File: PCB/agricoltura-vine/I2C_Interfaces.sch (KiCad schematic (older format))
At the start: 11 parts, among them T10 BM04B-SRSS-TB(LF)(SN), T11 BM04B-SRSS-TB(LF)(SN), T12 BM04B-SRSS-TB(LF)(SN), T13 BM04B-SRSS-TB(LF)(SN), T14 BM04B-SRSS-TB(LF)(SN), T15 BM04B-SRSS-TB(LF)(SN), T8 BM04B-SRSS-TB(LF)(SN), T9 BM04B-SRSS-TB(LF)(SN), U3 TCA9548APWR

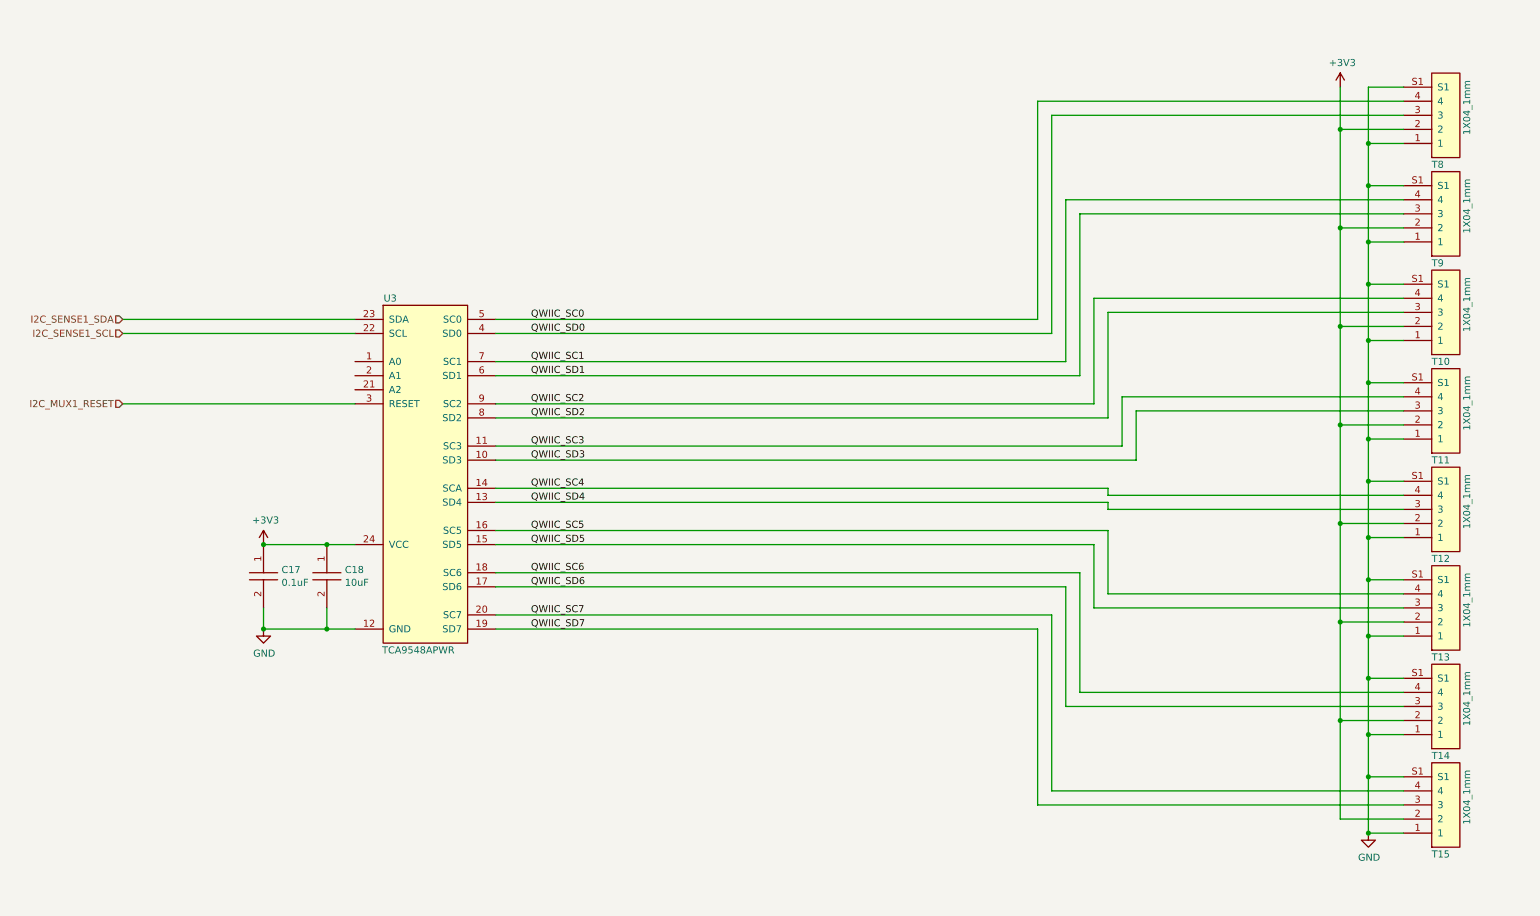
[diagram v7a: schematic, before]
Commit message: Added EEProm
Eeprom added and routed in circuit board, USB resitors added. TVS diodes and pullups added to I2C ports not yet placed.
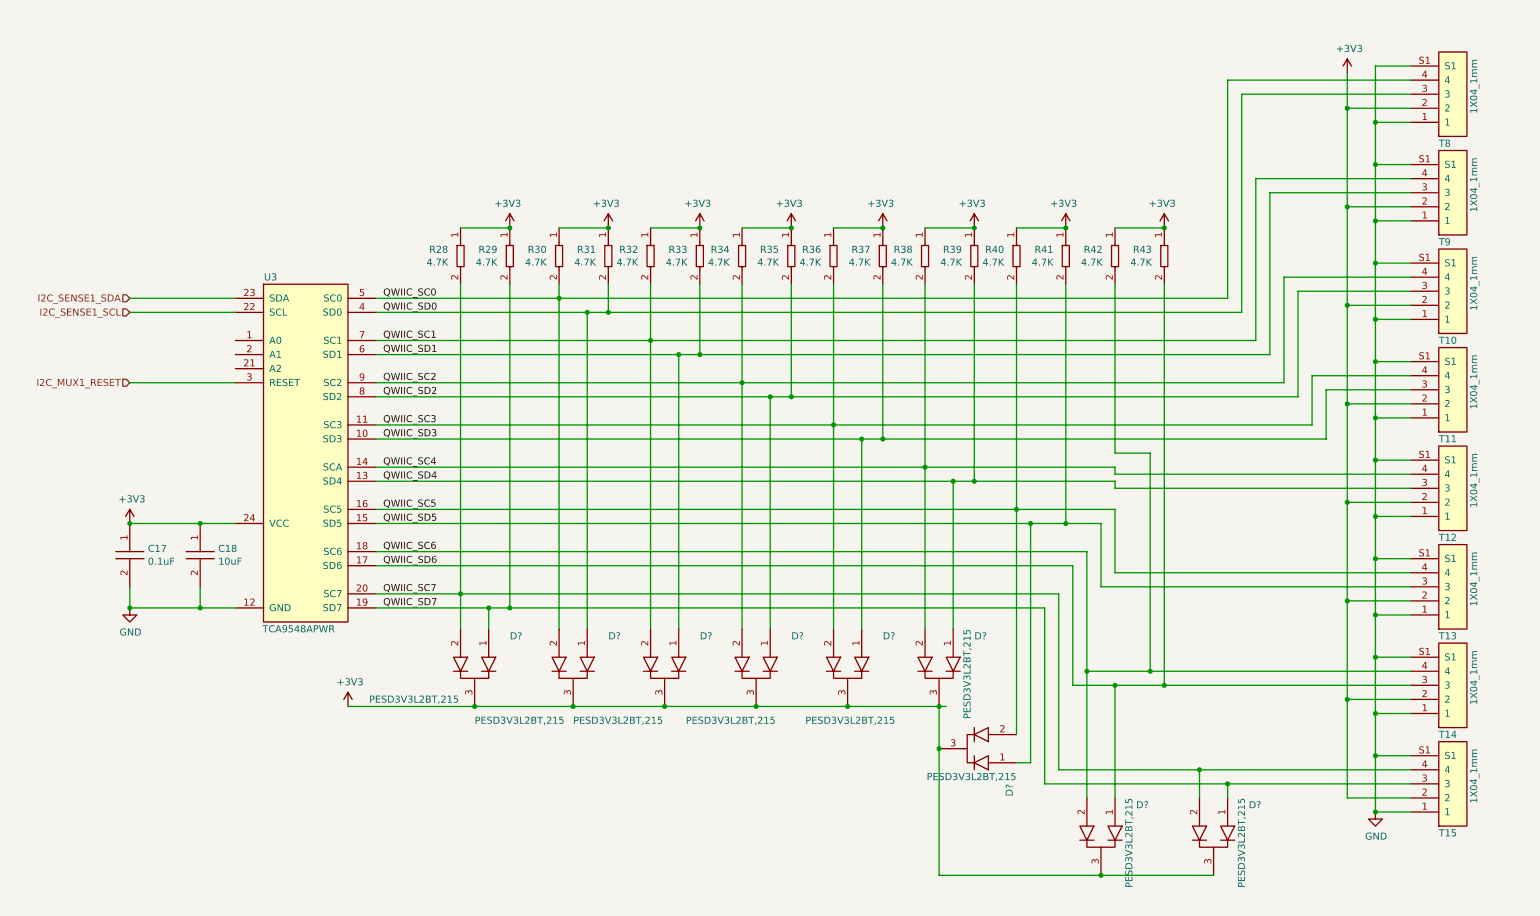
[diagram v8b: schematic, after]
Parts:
- added D? (x9): PESD3V3L2BT,215, AVR-KiCAD-Lib-Diodes:SOT-23, symbol AVR-KiCAD-Lib-Diodes:PESD3V3L2BT,215
- added R28, R29, R30, R31, R32, R33, R34, R35, R36, R37, R38, R39, R40, R41, R42, R43: RC0402FR-074K7L, AVR-KiCAD-Lib-Resistors:R0402, symbol AVR-KiCAD-Lib-Resistors:RC0402FR-074K7L
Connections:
- net +3V3: now also D?.3, D?.3, D?.3, D?.3, D?.3, D?.3, D?.3, D?.3, D?.3, R28.1, R29.1, R30.1, R31.1, R32.1, R33.1, R34.1, R35.1, R36.1, R37.1, R38.1, R39.1, R40.1, R41.1, R42.1, R43.1
- net QWIIC_SC0: now also D?.2, R30.2
- net QWIIC_SC1: now also D?.2, R32.2
- net QWIIC_SC2: now also D?.2, R34.2
- net QWIIC_SC3: now also D?.2, R36.2
- net QWIIC_SC4: now also D?.2, R38.2
- net QWIIC_SC5: now also D?.2, R40.2
- net QWIIC_SC6: now also D?.2, R42.2
- net QWIIC_SC7: now also D?.2, D?.2, R28.2
- net QWIIC_SD0: now also D?.1, R31.2
- net QWIIC_SD1: now also D?.1, R33.2
- net QWIIC_SD2: now also D?.1, R35.2
- net QWIIC_SD3: now also D?.1, R37.2
- net QWIIC_SD4: now also D?.1, R39.2
- net QWIIC_SD5: now also D?.1, R41.2
- net QWIIC_SD6: now also D?.1, R43.2
- net QWIIC_SD7: now also D?.1, D?.1, R29.2
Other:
- moved on the sheet: C17, C18, T10, T11, T12, T13, T14, T15, T8, T9, U3
